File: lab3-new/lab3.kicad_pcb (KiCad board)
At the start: 2 copper layers, 32 x 50.8 mm, 14 parts, among them J1 Conn_01x02_Male, J2 USB_A, U1 Regulator

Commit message: smd to tht
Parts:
- C1, C2: footprint Capacitor_SMD:C_0201_0603Metric -> Capacitor_THT:C_Disc_D3.0mm_W1.6mm_P2.50mm
- L1, L2: footprint Inductor_SMD:L_6.3x6.3_H3 -> Inductor_THT:L_Axial_L5.0mm_D3.6mm_P10.00mm_Horizontal_Murata_BL01RN1A2A2
- R1, R2, R3, R4: footprint Resistor_SMD:R_0201_0603Metric -> Resistor_THT:R_Axial_DIN0204_L3.6mm_D1.6mm_P1.90mm_Vertical

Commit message: Finished layout
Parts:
- F1: footprint Fuse:Fuse_0201_0603Metric -> Fuse:Fuse_BelFuse_0ZRE0005FF_L8.3mm_W3.8mm
- moved C1 16.1 mm to (86.1, 109.7)
- moved R1 13.7 mm to (104.6, 111.0), turned to 270 degrees
- moved J1 12.8 mm to (96.8, 122.7)
- moved L2 11.7 mm to (85.3, 93.2), turned to 270 degrees
- moved D2 11.7 mm to (85.3, 116.8)
- moved R4 11.0 mm to (97.0, 115.3)
- moved F1 10.8 mm to (90.7, 120.1), turned to 270 degrees
- moved R2 10.7 mm to (95.8, 94.2), turned to 180 degrees
- moved U1 10.5 mm to (93.2, 113.0)
- moved D1 7.89 mm to (103.4, 116.8), turned to 90 degrees
- moved J2 7.38 mm to (95.0, 81.0)
- moved L1 5.57 mm to (98.8, 100.8), turned to 180 degrees
- moved C2 1.61 mm to (99.6, 107.7), turned to 180 degrees
- moved R3 1.55 mm to (104.6, 105.4), turned to 180 degrees
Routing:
- net GND: track 0.00 -> 67.8 mm, vias 0 -> 2
- net +5V: track 0.00 -> 51.9 mm
- net Net-(D2-Pad1): track 0.00 -> 25.3 mm
- net Net-(C1-Pad1): track 0.00 -> 15.9 mm
- net Net-(R3-Pad2): track 0.00 -> 15.6 mm
- net Net-(J2-Pad5): track 0.00 -> 14.0 mm
- net Net-(F1-Pad2): track 0.00 -> 9.78 mm
- net Net-(C1-Pad2): track 0.00 -> 9.58 mm, vias 0 -> 1
- net Net-(D2-Pad2): track 0.00 -> 6.58 mm
- net Net-(D1-Pad2): track 0.00 -> 4.66 mm
- net Net-(J2-Pad3): track 0.00 -> 3.66 mm
- net Net-(J2-Pad2): track 0.00 -> 3.62 mm

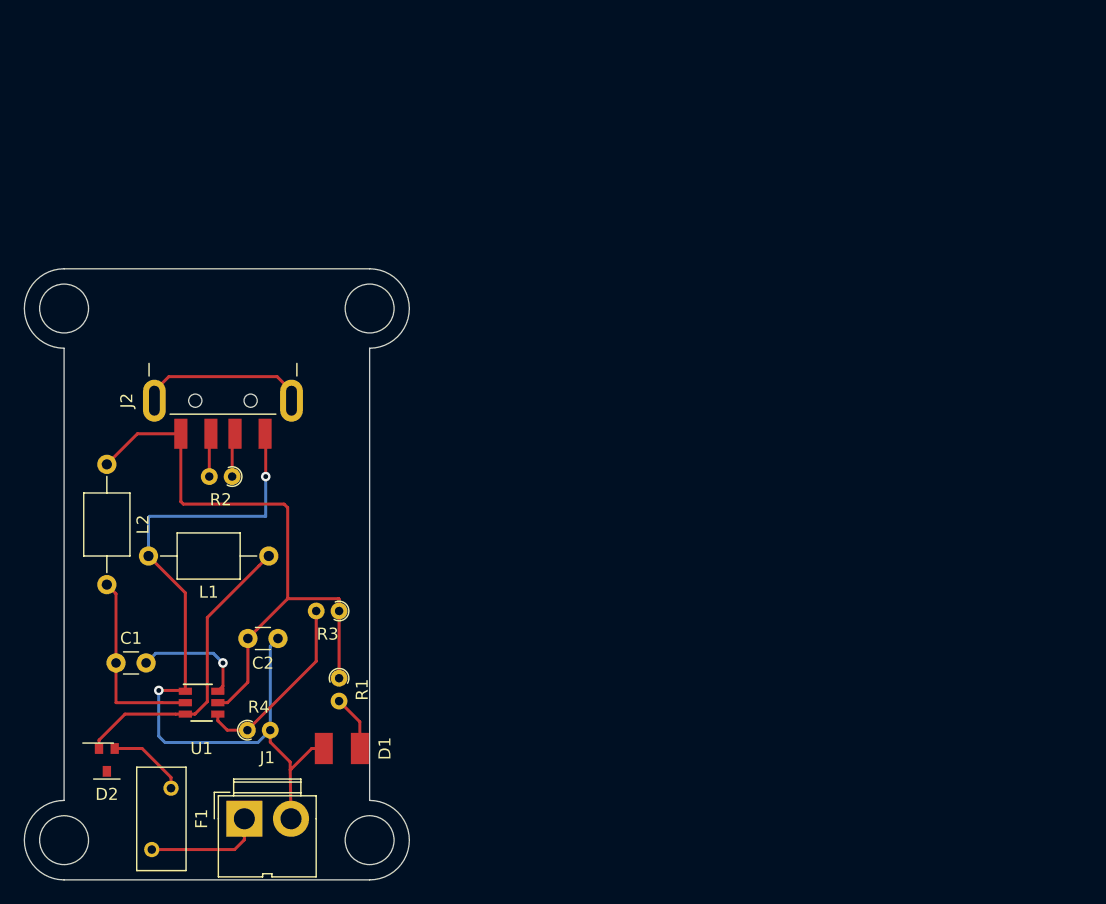
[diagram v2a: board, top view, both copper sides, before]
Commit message: changed diode footprint and assigned to schematic
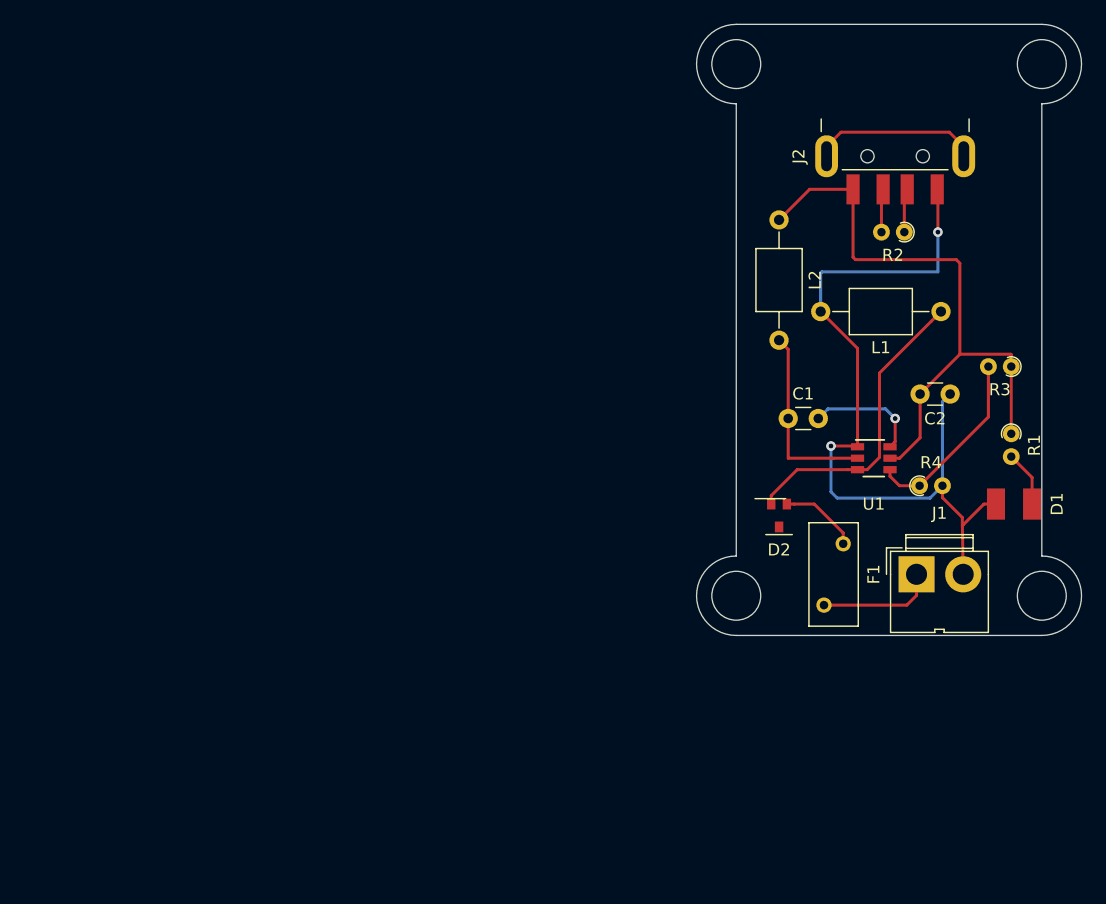
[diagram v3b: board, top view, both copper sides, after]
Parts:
- moved D1 59.5 mm to (159.3, 96.5)
- moved U1 59.5 mm to (149.1, 92.7)
- moved C1 59.5 mm to (142.0, 89.4)
- moved C2 59.5 mm to (155.4, 87.4)
- moved D2 59.5 mm to (141.2, 96.5)
- moved F1 59.5 mm to (146.6, 99.8)
- moved J1 59.5 mm to (152.7, 102.4)
- moved J2 59.5 mm to (150.9, 60.7)
- moved L1 59.5 mm to (154.7, 80.5)
- moved L2 59.5 mm to (141.2, 72.9)
- moved R1 59.5 mm to (160.5, 90.7)
- moved R2 59.5 mm to (151.6, 73.9)
- moved R3 59.5 mm to (160.5, 85.1)
- moved R4 59.5 mm to (152.9, 95.0)

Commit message: updated diode in layout
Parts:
- D2: footprint lab3-new:diode -> lab3-new:diode2
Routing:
- net Net-(D2-Pad1): track 25.3 -> 24.0 mm
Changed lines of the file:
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@@
     (thickness 1.6)
     (drawings 12)
-    (tracks 87)
+    (tracks 86)
     (zones 0)
     (modules 14)
@@
     )
   )
-  (module lab3-new:diode (layer F.Cu)
-    (at 141.224 96.52)
-    (fp_text reference D2 (at 0 3.81 unlocked) (layer F.SilkS)
-      (effects (font (size 1 1) (thickness 0.15)))
-    )
-    (fp_text value D_Schottky (at 0 -2.54 unlocked) (layer F.Fab)
-      (effects (font (size 1 1) (thickness 0.15)))
-    )
-    (fp_line (start -1.1 2.54) (end 1.1 2.54) (layer F.SilkS) (width 0.12))
-    (fp_line (start -2 -0.45) (end 0.55 -0.45) (layer F.SilkS) (width 0.12))
-    (fp_line (start 1.1 0.45) (end 1.1 1.45) (layer F.CrtYd) (width 0.12))
-    (fp_line (start -1.1 0.45) (end 1.1 0.45) (layer F.CrtYd) (width 0.12))
-    (fp_line (start -1.1 1.45) (end 1.1 1.45) (layer F.CrtYd) (width 0.12))
-    (fp_line (start -1.1 0.45) (end -1.1 1.45) (layer F.CrtYd) (width 0.12))
-    (pad 3 smd rect (at 0 1.9) (size 0.7 0.9) (layers F.Cu F.Paste F.Mask))
-    (pad 1 smd rect (at -0.65 0) (size 0.7 0.9) (layers F.Cu F.Paste F.Mask)
-      (net 6 "Net-(D2-Pad1)"))
-    (pad 2 smd rect (at 0.65 0) (size 0.7 0.9) (layers F.Cu F.Paste F.Mask)
-      (net 7 "Net-(D2-Pad2)"))
-  )
   (module lab3-new:led (layer F.Cu)
     (at 159.258 96.52 90)
@@
     (pad 1 smd rect (at 0 0 90) (size 2.6 1.5) (layers F.Cu F.Paste F.Mask)
       (net 4 GND))
+  )
+  (module lab3-new:diode2 (layer F.Cu)
+    (at 141.224 96.52)
+    (fp_text reference D2 (at 0 3.175) (layer F.SilkS)
+      (effects (font (size 1 1) (thickness 0.15)))
+    )
+    (fp_text value D_Schottky (at 0 -3.175) (layer F.Fab)
+      (effects (font (size 1 1) (thickness 0.15)))
+    )
+    (fp_line (start 0.675 -0.9) (end 0.675 0.9) (layer F.CrtYd) (width 0.12))
+    (fp_line (start 0.675 0.9) (end -0.675 0.9) (layer F.CrtYd) (width 0.12))
+    (fp_line (start -0.675 -0.9) (end -0.675 0.9) (layer F.CrtYd) (width 0.12))
+    (fp_line (start 0.675 -0.9) (end -0.675 -0.9) (layer F.CrtYd) (width 0.12))
+    (fp_line (start 0.675 -0.9) (end -0.9 -0.9) (layer F.SilkS) (width 0.12))
+    (fp_line (start 0.675 0.9) (end -0.675 0.9) (layer F.SilkS) (width 0.12))
+    (pad 1 smd rect (at 0 -1.1) (size 0.4 0.5) (layers F.Cu F.Paste F.Mask)
+      (net 6 "Net-(D2-Pad1)"))
+    (pad 2 smd rect (at 0 1.1) (size 0.4 0.5) (layers F.Cu F.Paste F.Mask)
+      (net 7 "Net-(D2-Pad2)"))
   )
   (gr_circle (center 163.068 59.944) (end 163.068 61.976) (layer Edge.Cuts) (width 0.05))
@@
   (segment (start 150.076001 88.608001) (end 150.876 89.408) (width 0.25) (layer B.Cu) (net 1))
   (segment (start 150.876 89.408) (end 150.876 89.408) (width 0.25) (layer B.Cu) (net 1))
-  (via (at 150.876 89.408) (size 0.8) (drill 0.4) (layers F.Cu B.Cu) (net 1) (status 1000000))
+  (via (at 150.876 89.408) (size 0.8) (drill 0.4) (layers F.Cu B.Cu) (net 1))
   (segment (start 150.876 91.332) (end 150.448 91.76) (width 0.25) (layer F.Cu) (net 1))
   (segment (start 150.876 89.408) (end 150.876 91.332) (width 0.25) (layer F.Cu) (net 1))
@@
   (segment (start 162.258 94.308) (end 160.528 92.578) (width 0.25) (layer F.Cu) (net 5))
   (segment (start 162.258 96.52) (end 162.258 94.308) (width 0.25) (layer F.Cu) (net 5))
-  (segment (start 146.948 93.66) (end 147.748 93.66) (width 0.25) (layer F.Cu) (net 6))
-  (segment (start 140.574 95.82) (end 142.734 93.66) (width 0.25) (layer F.Cu) (net 6))
-  (segment (start 142.734 93.66) (end 146.948 93.66) (width 0.25) (layer F.Cu) (net 6))
-  (segment (start 140.574 96.52) (end 140.574 95.82) (width 0.25) (layer F.Cu) (net 6))
   (segment (start 149.572999 92.635001) (end 149.572999 85.631001) (width 0.25) (layer F.Cu) (net 6))
   (segment (start 149.572999 85.631001) (end 153.886001 81.317999) (width 0.25) (layer F.Cu) (net 6))
@@
   (segment (start 153.886001 81.317999) (end 154.686 80.518) (width 0.25) (layer F.Cu) (net 6))
   (segment (start 147.748 93.66) (end 148.548 93.66) (width 0.25) (layer F.Cu) (net 6))
-  (segment (start 144.154025 96.52) (end 142.474 96.52) (width 0.25) (layer F.Cu) (net 7))
-  (segment (start 142.474 96.52) (end 141.874 96.52) (width 0.25) (layer F.Cu) (net 7))
-  (segment (start 146.558 98.923975) (end 144.154025 96.52) (width 0.25) (layer F.Cu) (net 7))
-  (segment (start 146.558 99.822) (end 146.558 98.923975) (width 0.25) (layer F.Cu) (net 7))
+  (segment (start 146.948 93.66) (end 147.748 93.66) (width 0.25) (layer F.Cu) (net 6))
+  (segment (start 142.484 93.66) (end 146.948 93.66) (width 0.25) (layer F.Cu) (net 6))
+  (segment (start 141.224 94.92) (end 142.484 93.66) (width 0.25) (layer F.Cu) (net 6))
+  (segment (start 141.224 95.42) (end 141.224 94.92) (width 0.25) (layer F.Cu) (net 6))
+  (segment (start 141.224 98.12) (end 141.224 97.62) (width 0.25) (layer F.Cu) (net 7))
+  (segment (start 142.926 99.822) (end 141.224 98.12) (width 0.25) (layer F.Cu) (net 7))
+  (segment (start 146.558 99.822) (end 142.926 99.822) (width 0.25) (layer F.Cu) (net 7))
   (segment (start 151.844 104.922) (end 152.654 104.112) (width 0.25) (layer F.Cu) (net 8))
   (segment (start 152.654 104.112) (end 152.654 102.362) (width 0.25) (layer F.Cu) (net 8))

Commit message: finished circuit
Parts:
- added J3: Conn_01x01_Male, lab3-new:connector1, F.Cu at (163.1, 104.1)
- J1: value Conn_01x02_Male -> Conn_01x01_Male; footprint Connector:JWT_A3963_1x02_P3.96mm_Vertical -> lab3-new:connector1
- moved J1 15.1 mm to (137.7, 104.1)
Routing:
- net Net-(F1-Pad2): track 9.78 -> 5.04 mm
- net GND: track 67.8 -> 72.5 mm
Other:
- rule pad_to_mask_clearance: 0.051 -> 0.0508
- rule solder_mask_min_width: 0.25 -> 0.0762
- rule trace_min: 0.2 -> 0.1524
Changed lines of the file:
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@@
     (thickness 1.6)
     (drawings 12)
-    (tracks 86)
+    (tracks 88)
     (zones 0)
-    (modules 14)
+    (modules 15)
     (nets 13)
   )
@@
     (zone_clearance 0.508)
     (zone_45_only no)
-    (trace_min 0.2)
+    (trace_min 0.1524)
     (via_size 0.8)
     (via_drill 0.4)
@@
     (pad_size 1.524 1.524)
     (pad_drill 0.762)
-    (pad_to_mask_clearance 0.051)
-    (solder_mask_min_width 0.25)
+    (pad_to_mask_clearance 0.0508)
+    (solder_mask_min_width 0.0762)
     (aux_axis_origin 0 0)
     (visible_elements 7FFFFFFF)
@@
     )
   )
-  (module Connector:JWT_A3963_1x02_P3.96mm_Vertical (layer F.Cu)
-    (at 152.654 102.362)
-    (descr "JWT A3963, 3.96mm pitch Pin head connector (http://www.jwt.com.tw/pro_pdf/A3963.pdf)")
-    (tags "connector JWT A3963 pinhead")
-    (fp_text reference J1 (at 1.91 -5.08) (layer F.SilkS)
-      (effects (font (size 1 1) (thickness 0.15)))
-    )
-    (fp_text value Conn_01x02_Male (at 1.91 6.35) (layer F.Fab)
-      (effects (font (size 1 1) (thickness 0.15)))
-    )
-    (fp_line (start 5.97 4.83) (end 5.97 0) (layer F.SilkS) (width 0.12))
-    (fp_line (start -2.16 0) (end -2.16 4.83) (layer F.SilkS) (width 0.12))
-    (fp_line (start -2.16 -1.91) (end 5.97 -1.91) (layer F.SilkS) (width 0.12))
-    (fp_line (start -0.89 -1.91) (end -0.89 -3.3) (layer F.SilkS) (width 0.12))
-    (fp_line (start 4.7 -1.91) (end 4.7 -3.3) (layer F.SilkS) (width 0.12))
-    (fp_line (start -0.89 -3.3) (end 4.7 -3.3) (layer F.SilkS) (width 0.12))
-    (fp_line (start -2.16 -1.91) (end -2.16 0) (layer F.SilkS) (width 0.12))
-    (fp_line (start 5.97 -1.91) (end 5.97 0) (layer F.SilkS) (width 0.12))
-    (fp_line (start -0.89 -3.05) (end 4.7 -3.05) (layer F.SilkS) (width 0.12))
-    (fp_line (start -0.89 -2.16) (end 4.7 -2.16) (layer F.SilkS) (width 0.12))
-    (fp_line (start 2.29 4.57) (end 2.29 4.83) (layer F.SilkS) (width 0.12))
-    (fp_line (start 1.52 4.57) (end 2.29 4.57) (layer F.SilkS) (width 0.12))
-    (fp_line (start 1.52 4.83) (end 1.52 4.57) (layer F.SilkS) (width 0.12))
-    (fp_line (start 1.52 4.83) (end -2.16 4.83) (layer F.SilkS) (width 0.12))
-    (fp_line (start 2.29 4.83) (end 5.97 4.83) (layer F.SilkS) (width 0.12))
-    (fp_line (start -2.5 5.05) (end -2.5 -3.55) (layer F.CrtYd) (width 0.05))
-    (fp_line (start 6.35 5.05) (end -2.5 5.05) (layer F.CrtYd) (width 0.05))
-    (fp_line (start 6.35 -3.55) (end 6.35 5.05) (layer F.CrtYd) (width 0.05))
-    (fp_line (start -2.5 -3.55) (end 6.35 -3.55) (layer F.CrtYd) (width 0.05))
-    (fp_line (start -2.05 -1.8) (end 5.85 -1.8) (layer F.Fab) (width 0.1))
-    (fp_line (start 5.85 -1.8) (end 5.85 4.7) (layer F.Fab) (width 0.1))
-    (fp_line (start 5.85 4.7) (end -2.05 4.7) (layer F.Fab) (width 0.1))
-    (fp_line (start -2.05 4.7) (end -2.05 -1.8) (layer F.Fab) (width 0.1))
-    (fp_line (start -1.2 -2.2) (end -2.5 -2.2) (layer F.SilkS) (width 0.12))
-    (fp_line (start -2.5 -2.2) (end -2.5 0) (layer F.SilkS) (width 0.12))
-    (fp_line (start -1.25 -1.8) (end 0 -0.3) (layer F.Fab) (width 0.1))
-    (fp_line (start 0 -0.3) (end 1.25 -1.8) (layer F.Fab) (width 0.1))
-    (fp_line (start -0.8 -1.8) (end -0.8 -3.2) (layer F.Fab) (width 0.1))
-    (fp_line (start -0.8 -3.2) (end 4.6 -3.2) (layer F.Fab) (width 0.1))
-    (fp_line (start 4.6 -3.2) (end 4.6 -1.8) (layer F.Fab) (width 0.1))
-    (fp_text user %R (at 2.2 3.7) (layer F.Fab)
-      (effects (font (size 1 1) (thickness 0.15)))
-    )
-    (pad 2 thru_hole circle (at 3.88 0) (size 3 3) (drill 1.75) (layers *.Cu *.Mask)
-      (net 4 GND))
-    (pad 1 thru_hole rect (at 0 0) (size 3 3) (drill 1.75) (layers *.Cu *.Mask)
-      (net 8 "Net-(F1-Pad2)"))
-    (model ${KISYS3DMOD}/Connector.3dshapes/JWT_A3963_1x02_P3.96mm_Vertical.wrl
-      (at (xyz 0 0 0))
-      (scale (xyz 1 1 1))
-      (rotate (xyz 0 0 0))
-    )
-  )
   (module lab3-new:led (layer F.Cu)
     (at 159.258 96.52 90)
@@
       (effects (font (size 1 1) (thickness 0.15)))
     )
+    (fp_line (start 0.675 0.9) (end -0.675 0.9) (layer F.SilkS) (width 0.12))
+    (fp_line (start 0.675 -0.9) (end -0.9 -0.9) (layer F.SilkS) (width 0.12))
+    (fp_line (start 0.675 -0.9) (end -0.675 -0.9) (layer F.CrtYd) (width 0.12))
+    (fp_line (start -0.675 -0.9) (end -0.675 0.9) (layer F.CrtYd) (width 0.12))
+    (fp_line (start 0.675 0.9) (end -0.675 0.9) (layer F.CrtYd) (width 0.12))
     (fp_line (start 0.675 -0.9) (end 0.675 0.9) (layer F.CrtYd) (width 0.12))
-    (fp_line (start 0.675 0.9) (end -0.675 0.9) (layer F.CrtYd) (width 0.12))
-    (fp_line (start -0.675 -0.9) (end -0.675 0.9) (layer F.CrtYd) (width 0.12))
-    (fp_line (start 0.675 -0.9) (end -0.675 -0.9) (layer F.CrtYd) (width 0.12))
-    (fp_line (start 0.675 -0.9) (end -0.9 -0.9) (layer F.SilkS) (width 0.12))
-    (fp_line (start 0.675 0.9) (end -0.675 0.9) (layer F.SilkS) (width 0.12))
+    (pad 2 smd rect (at 0 1.1) (size 0.4 0.5) (layers F.Cu F.Paste F.Mask)
+      (net 7 "Net-(D2-Pad2)"))
     (pad 1 smd rect (at 0 -1.1) (size 0.4 0.5) (layers F.Cu F.Paste F.Mask)
       (net 6 "Net-(D2-Pad1)"))
-    (pad 2 smd rect (at 0 1.1) (size 0.4 0.5) (layers F.Cu F.Paste F.Mask)
-      (net 7 "Net-(D2-Pad2)"))
+  )
+  (module lab3-new:connector1 (layer F.Cu)
+    (at 137.668 104.14)
+    (fp_text reference J1 (at 0 3.8) (layer F.SilkS)
+      (effects (font (size 1 1) (thickness 0.15)))
+    )
+    (fp_text value Conn_01x01_Male (at 0 -3.6) (layer F.Fab)
+      (effects (font (size 1 1) (thickness 0.15)))
+    )
+    (fp_circle (center 0 0) (end 0.16 0) (layer F.CrtYd) (width 0.01))
+    (pad 1 thru_hole circle (at 0 0) (size 5.842 5.842) (drill 4.064) (layers *.Cu *.Mask)
+      (net 8 "Net-(F1-Pad2)"))
+  )
+  (module lab3-new:connector1 (layer F.Cu)
+    (at 163.068 104.14)
+    (fp_text reference J3 (at 0 3.8) (layer F.SilkS)
+      (effects (font (size 1 1) (thickness 0.15)))
+    )
+    (fp_text value Conn_01x01_Male (at 0 -3.6) (layer F.Fab)
+      (effects (font (size 1 1) (thickness 0.15)))
+    )
+    (fp_circle (center 0 0) (end 0.16 0) (layer F.CrtYd) (width 0.01))
+    (pad 1 thru_hole circle (at 0 0) (size 5.842 5.842) (drill 4.064) (layers *.Cu *.Mask)
+      (net 4 GND))
   )
   (gr_circle (center 163.068 59.944) (end 163.068 61.976) (layer Edge.Cuts) (width 0.05))
@@
   (segment (start 145.542 95.504) (end 145.542 91.694) (width 0.25) (layer B.Cu) (net 4))
   (segment (start 145.542 91.694) (end 145.542 91.694) (width 0.25) (layer B.Cu) (net 4))
-  (via (at 145.542 91.694) (size 0.8) (drill 0.4) (layers F.Cu B.Cu) (net 4))
+  (via (at 145.542 91.694) (size 0.8) (drill 0.4) (layers F.Cu B.Cu) (net 4) (status 1000000))
   (segment (start 147.682 91.694) (end 147.748 91.76) (width 0.25) (layer F.Cu) (net 4))
   (segment (start 145.542 91.694) (end 147.682 91.694) (width 0.25) (layer F.Cu) (net 4))
@@
   (segment (start 156.464 98.298) (end 156.534 98.244) (width 0.25) (layer F.Cu) (net 4))
   (segment (start 156.534 102.362) (end 156.464 98.298) (width 0.25) (layer F.Cu) (net 4))
+  (segment (start 160.274 102.362) (end 160.951408 103.039409) (width 0.25) (layer F.Cu) (net 4))
+  (segment (start 156.534 102.362) (end 160.274 102.362) (width 0.25) (layer F.Cu) (net 4))
   (segment (start 162.258 94.308) (end 160.528 92.578) (width 0.25) (layer F.Cu) (net 5))
   (segment (start 162.258 96.52) (end 162.258 94.308) (width 0.25) (layer F.Cu) (net 5))
@@
   (segment (start 142.926 99.822) (end 141.224 98.12) (width 0.25) (layer F.Cu) (net 7))
   (segment (start 146.558 99.822) (end 142.926 99.822) (width 0.25) (layer F.Cu) (net 7))
-  (segment (start 151.844 104.922) (end 152.654 104.112) (width 0.25) (layer F.Cu) (net 8))
-  (segment (start 152.654 104.112) (end 152.654 102.362) (width 0.25) (layer F.Cu) (net 8))
-  (segment (start 144.958 104.922) (end 151.844 104.922) (width 0.25) (layer F.Cu) (net 8))
+  (segment (start 141.498 104.922) (end 139.974 104.922) (width 0.25) (layer F.Cu) (net 8))
+  (segment (start 144.958 104.922) (end 141.498 104.922) (width 0.25) (layer F.Cu) (net 8))
+  (segment (start 139.974 104.922) (end 139.934298 104.882298) (width 0.25) (layer F.Cu) (net 8))
   (segment (start 156.576 66.806) (end 156.576 67.606) (width 0.25) (layer F.Cu) (net 9))
   (segment (start 155.376 65.606) (end 156.576 66.806) (width 0.25) (layer F.Cu) (net 9))
